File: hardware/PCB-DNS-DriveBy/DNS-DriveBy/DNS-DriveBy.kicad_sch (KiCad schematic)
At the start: 11 parts, among them J1 JST 2.0, Q1 2N3904, Q2 2N3904, SW1 SW_SPST, U1 NEO-6M, U2 D1 Mini

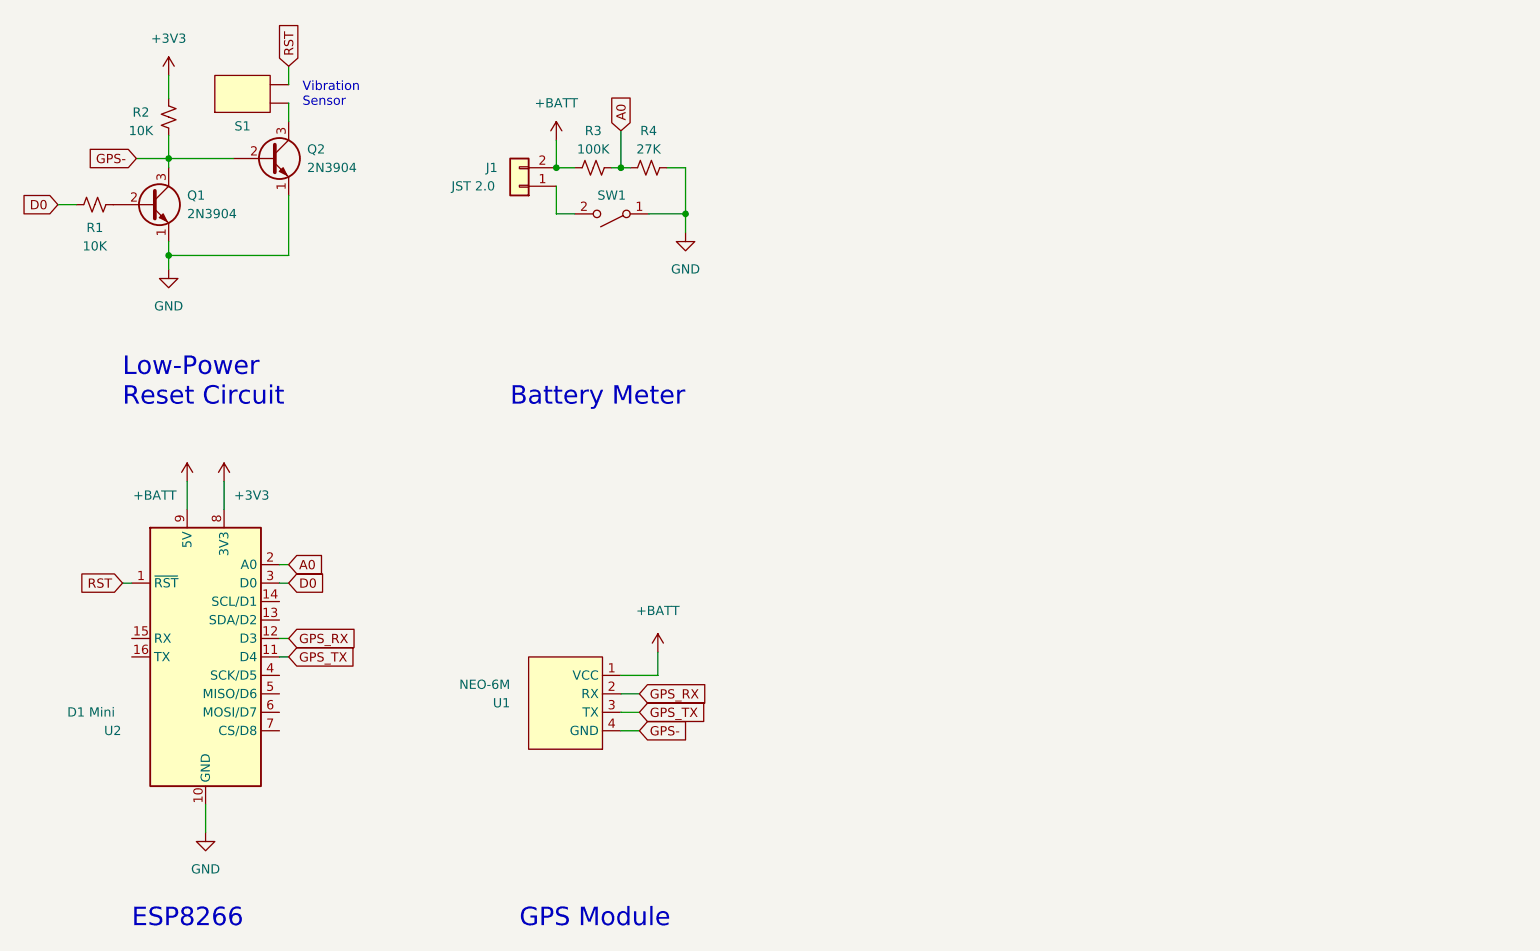
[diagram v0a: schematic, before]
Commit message: PCB improvements: screen + serial breakout, re-routeable GPS pins
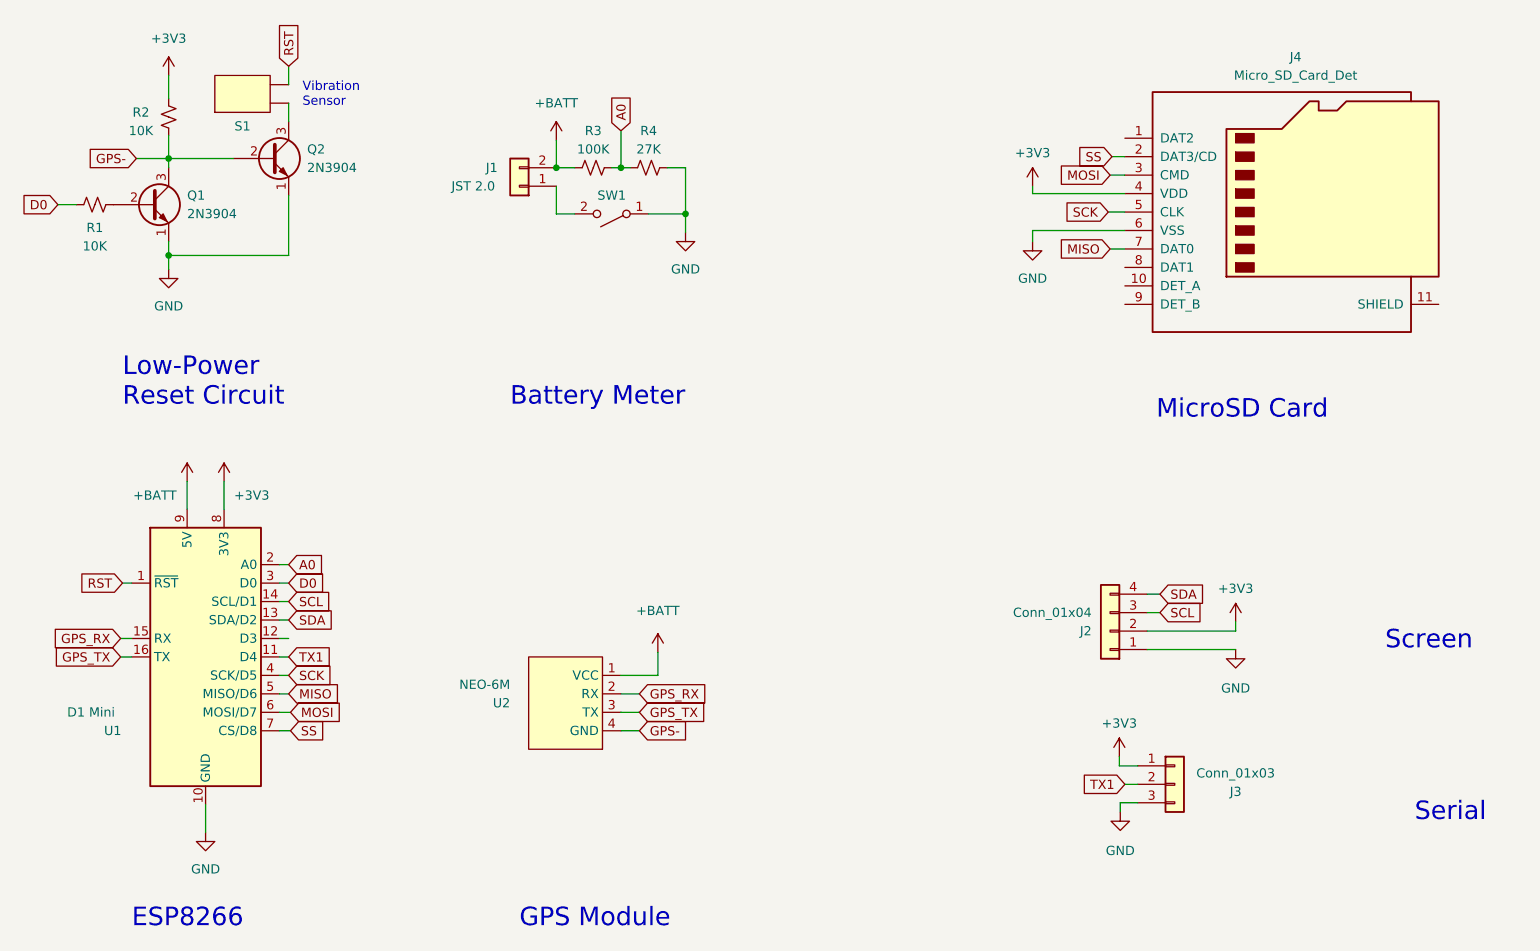
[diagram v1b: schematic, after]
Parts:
- added J2: Conn_01x04, Connector_PinHeader_2.54mm:PinHeader_1x04_P2.54mm_Vertical, symbol Connector_Generic:Conn_01x04
- added J3: Conn_01x03, Connector_PinHeader_2.54mm:PinHeader_1x03_P2.54mm_Vertical, symbol Connector_Generic:Conn_01x03
- added J4: Micro_SD_Card_Det, symbol Connector:Micro_SD_Card_Det
- renumbered U2 to U1, U1 to U2
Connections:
- net +3V3: now also J2.2 (Pin_2), J3.1 (Pin_1), J4.4 (VDD)
- net GND: now also J2.1 (Pin_1), J3.3 (Pin_3), J4.6 (VSS)
- net GPS_RX: now also U1.15 (RX); no longer U1.12 (D3)
- net GPS_TX: now also U1.16 (TX); no longer U1.11 (D4)
- net SDA: now reaches U1.13 (SDA/D2)
- net SDA: now also J2.4 (Pin_4)
- net SCL: now reaches U1.14 (SCL/D1)
- net SCL: now also J2.3 (Pin_3)
- net SCK: now reaches U1.4 (SCK/D5)
- net SCK: now also J4.5 (CLK)
- net MISO: now reaches U1.5 (MISO/D6)
- net MISO: now also J4.7 (DAT0)
- net MOSI: now reaches U1.6 (MOSI/D7)
- net MOSI: now also J4.3 (CMD)
- net SS: now reaches U1.7 (CS/D8)
- net SS: now also J4.2 (DAT3/CD)
- new net TX1: J3.2 (Pin_2), U1.11 (D4)
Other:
- note added: "MicroSD Card"
- note added: "Screen"
- note added: "Serial"

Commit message: fix low-power mode hardware, add jumper pads, graphics
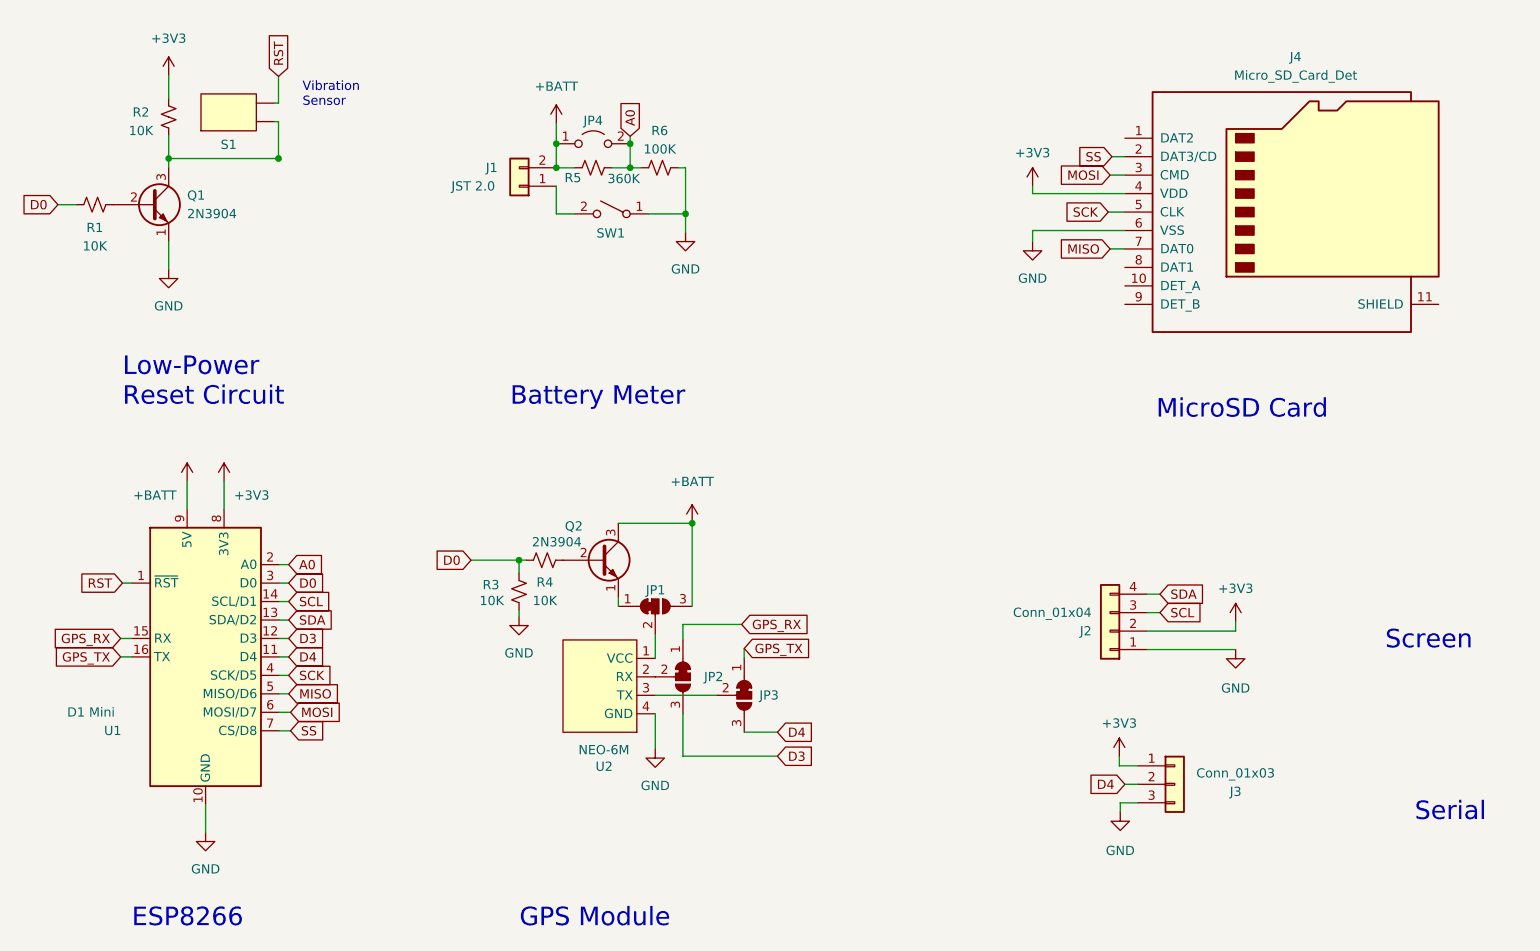
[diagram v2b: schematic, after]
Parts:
- added JP1, JP2, JP3: SolderJumper_3_Bridged12, Jumper:SolderJumper-3_P1.3mm_Bridged12_Pad1.0x1.5mm, symbol Jumper:SolderJumper_3_Bridged12
- added JP4: Jumper_2_Open, Jumper:SolderJumper-2_P1.3mm_Open_Pad1.0x1.5mm, symbol Jumper:Jumper_2_Open
- added R3, R4: 10K, Resistor_THT:R_Axial_DIN0207_L6.3mm_D2.5mm_P7.62mm_Horizontal, symbol Device:R_Small_US
- R5: renamed from R3; value 100K -> 360K
- R6: renamed from R4; value 27K -> 100K
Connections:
- net +BATT: now also Q2.3 (C), JP1.3 (B), JP4.1 (A); no longer U2.1 (VCC)
- net A0: now also JP4.2 (B)
- net D0: now also R3.2, R4.2
- net GND: now also U2.4 (GND), R3.1; no longer Q2.1 (E)
- net GPS_RX: now also JP2.1 (A); no longer U2.2 (RX)
- net GPS_TX: now also JP3.1 (A); no longer U2.3 (TX)
- net D3: now reaches U1.12 (D3)
- net D3: now also JP2.3 (B)
- net GPS-: no longer names the net of Q1.3 (C), R2.1
- net GPS-: now also S1.; no longer Q2.2 (B), U2.4 (GND)
- net TX1 renamed D4
- net D4: now also JP3.3 (B)
- new net: JP2.2 (C), U2.2 (RX)
- new net: JP1.1 (A), Q2.1 (E)
- new net: JP1.2 (C), U2.1 (VCC)
- new net: JP3.2 (C), U2.3 (TX)
- new net: Q2.2 (B), R4.1
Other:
- moved on the sheet: R6, S1, SW1, U2
